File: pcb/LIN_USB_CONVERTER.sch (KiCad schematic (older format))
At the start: 33 parts, among them J1 Conn_01x03, J2 TerminalBlock, J3 GS2, J4 USB_A, J5 Conn_01x02, P2 CONN_01X05, U1 TJA1028TK/3V3/20/J, U2 MAX12931BASA+, U3 MCP1700T-3302E/TT, U4 STM32F042G4U6

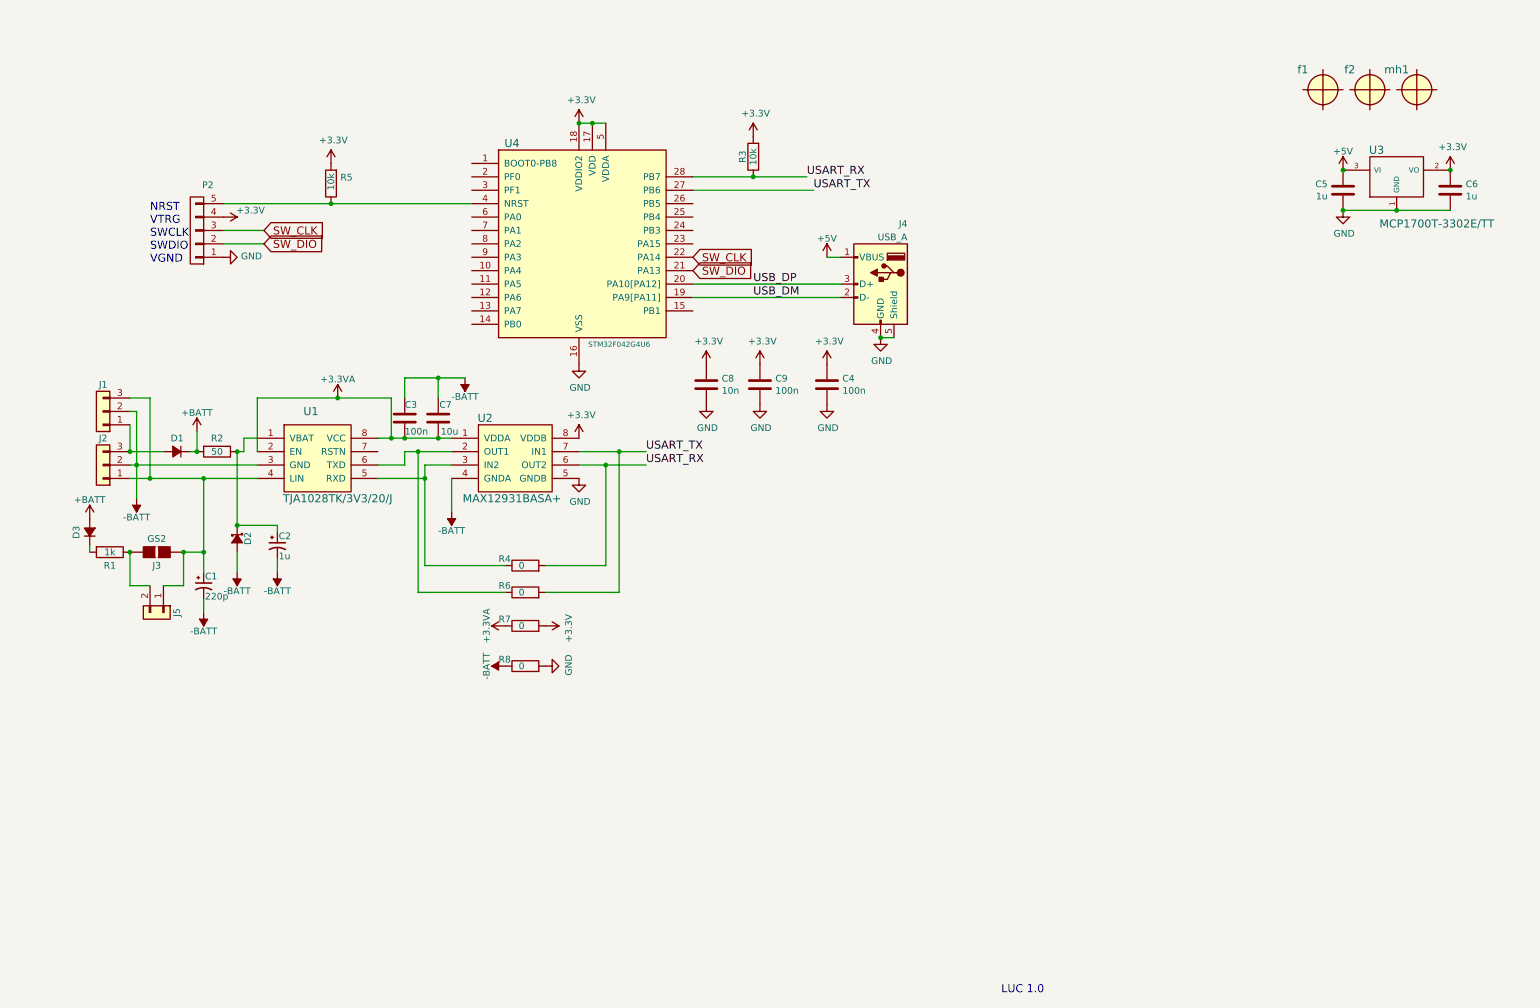
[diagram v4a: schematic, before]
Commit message: Remove of galvanic spearator
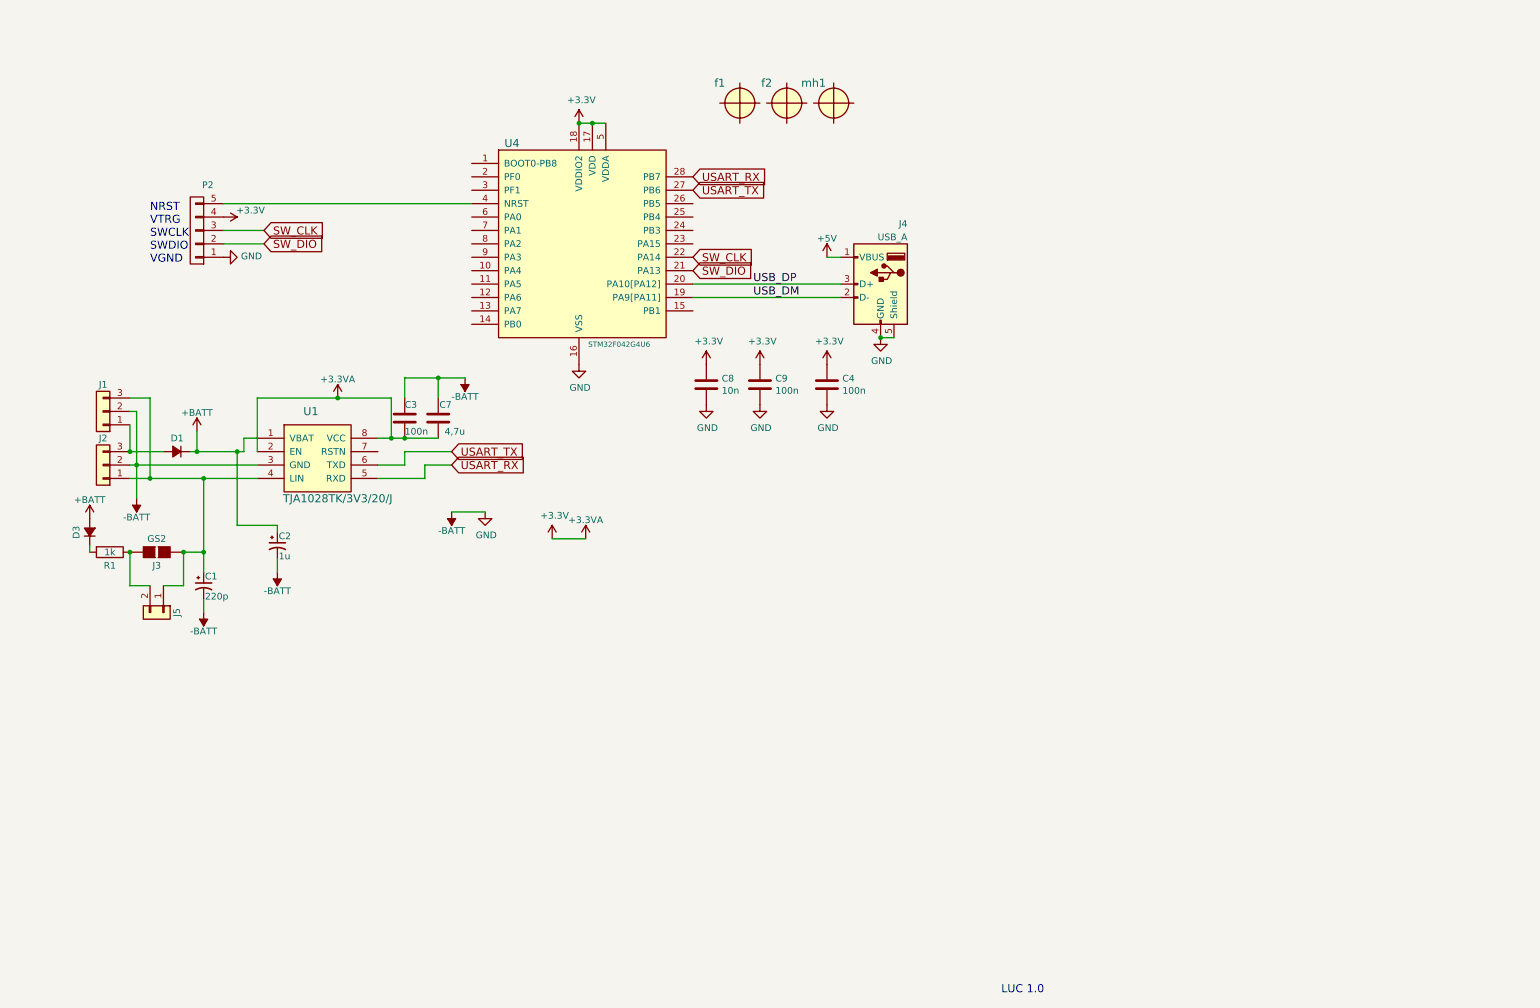
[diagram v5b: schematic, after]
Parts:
- removed C5, C6: 1u, Capacitors_SMD:C_0402, symbol LIN_USB_CONVERTER-rescue:C-RESCUE-LIN_USB_CONVERTER
- removed D2: 1N5819HW-7-F, Diodes_SMD:D_SOT-23_ANK, symbol LIN_USB_CONVERTER-rescue:D_Schottky_Small_ALT-RESCUE-LIN_USB_CONVERTER
- removed R2: 50, Resistors_SMD:R_0603, symbol LIN_USB_CONVERTER-rescue:R-RESCUE-LIN_USB_CONVERTER
- removed R3, R5: 10k, Resistors_SMD:R_0603, symbol LIN_USB_CONVERTER-rescue:R-RESCUE-LIN_USB_CONVERTER
- removed R4, R6, R7, R8: 0, Resistors_SMD:R_0603, symbol LIN_USB_CONVERTER-rescue:R-RESCUE-LIN_USB_CONVERTER
- removed U2: MAX12931BASA+, usb_ccb_custom:SOIC-8-N_MAXIM, symbol LIN_USB_CONVERTER-rescue:MAX12931-RESCUE-LIN_USB_CONVERTER
- removed U3: MCP1700T-3302E/TT, TO_SOT_Packages_SMD:SOT-23, symbol LIN_USB_CONVERTER-rescue:MCP1700T-3302E_TT-RESCUE-LIN_USB_CONVERTER
- C2: footprint Capacitors_SMD:C_0603 -> Capacitors_SMD:C_0805
- C7: value 10u -> 4,7u
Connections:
- net +3V3 is gone; now on net +3.3VA: C4.1, C8.1, C9.1, P2.4 (P4), U4.17 (VDD), U4.18 (VDDIO2), U4.5 (VDDA)
- net GND is gone; now on net -BATT: C4.2, C8.2, C9.2, J4.4 (GND), J4.5 (Shield), P2.1 (P1), U4.16 (VSS)
- net +BATT: now also C2.1, U1.1 (VBAT)
- net USART_RX: now also U1.5 (RXD)
- net USART_TX: now also U1.6 (TXD)
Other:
- moved on the sheet: f1, f2, mh1

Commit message: TJA package update
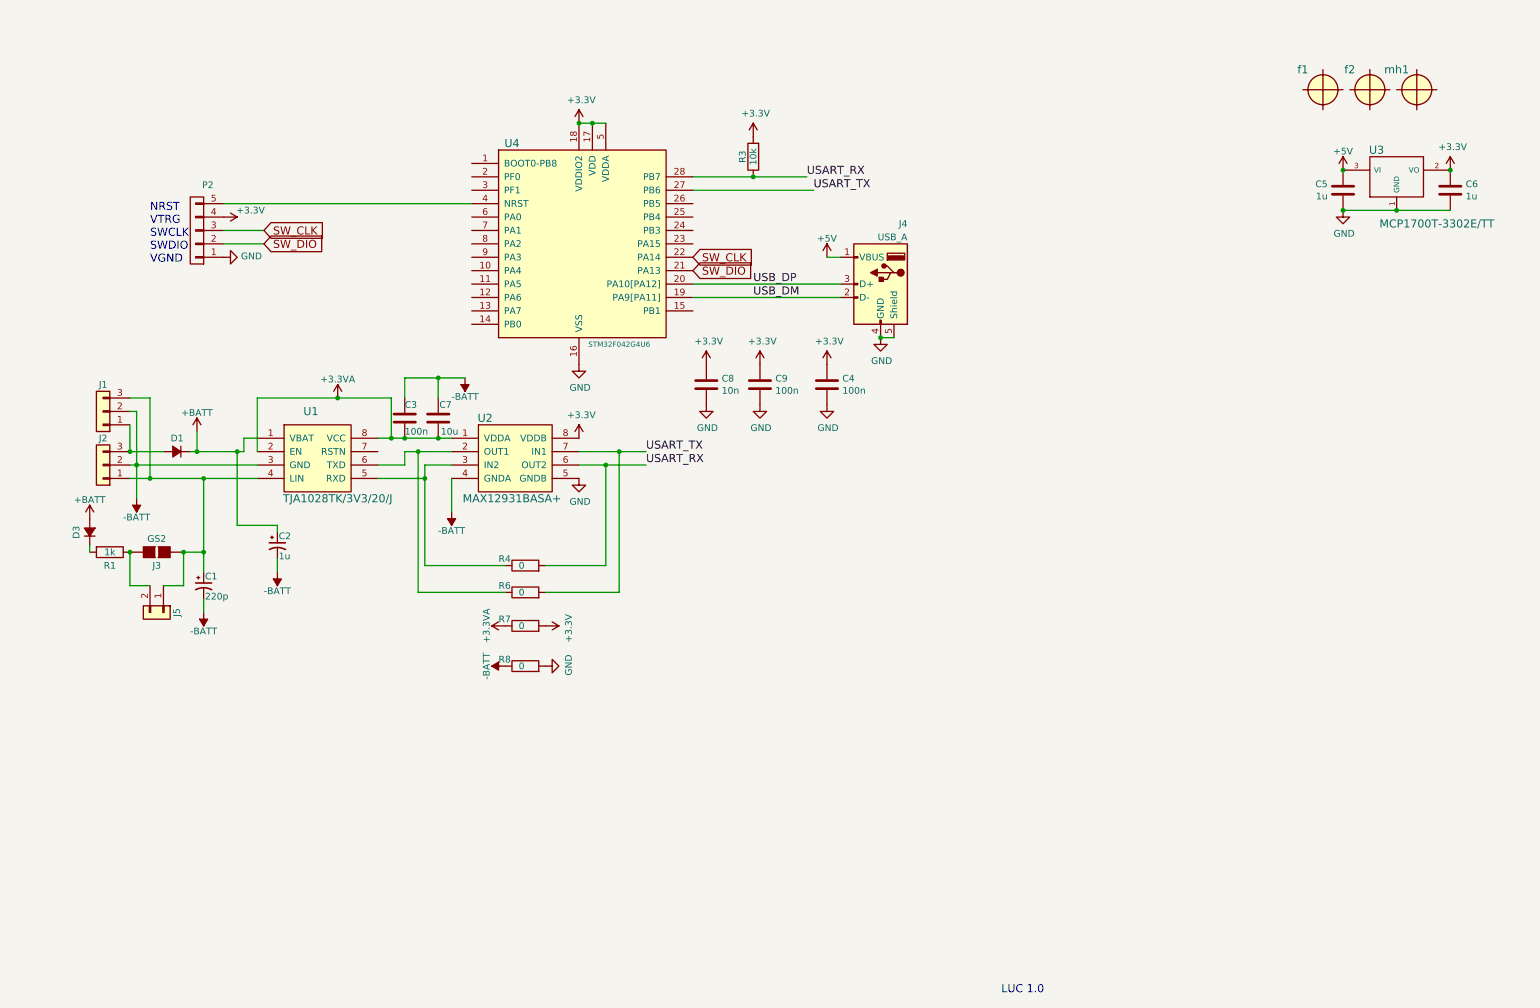
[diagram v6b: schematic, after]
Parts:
- added C5, C6: 1u, Capacitors_SMD:C_0603, symbol LIN_USB_CONVERTER-rescue:C-RESCUE-LIN_USB_CONVERTER
- added R3: 10k, Resistors_SMD:R_0603, symbol LIN_USB_CONVERTER-rescue:R-RESCUE-LIN_USB_CONVERTER
- added R4, R6, R7, R8: 0, Resistors_SMD:R_0603, symbol LIN_USB_CONVERTER-rescue:R-RESCUE-LIN_USB_CONVERTER
- added U2: MAX12931BASA+, usb_ccb_custom:SOIC-8-N_MAXIM, symbol LIN_USB_CONVERTER-rescue:MAX12931-RESCUE-LIN_USB_CONVERTER
- added U3: MCP1700T-3302E/TT, TO_SOT_Packages_SMD:SOT-23, symbol LIN_USB_CONVERTER-rescue:MCP1700T-3302E_TT-RESCUE-LIN_USB_CONVERTER
- C3, C4, C8, C9: footprint Capacitors_SMD:C_0402 -> Capacitors_SMD:C_0603
- C7: value 4,7u -> 10u; footprint Capacitors_SMD:C_0603 -> Capacitors_SMD:C_0805; 1st Disrtib Link https://www.tme.eu/pl/details/cl05a106mq5nunc/kondensatory-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 -> (none); Manufacturer SAMSUNG/CL05A106MQ5NUNC -> (none)
- U1: footprint usb_ccb_custom:HVSON8 -> Housings_SOIC:SOIC-8_3.9x4.9mm_Pitch1.27mm; 1st Disrtib Link https://octopart.com/tja1028tk%2F3v3%2F20%2Fj-nxp+semicondu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 -> (none)
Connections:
- net +3.3VA: now also R7.1, U2.1 (VDDA); no longer C4.1, C8.1, C9.1, P2.4 (P4), U4.17 (VDD), U4.18 (VDDIO2), U4.5 (VDDA)
- net +5V: now also C5.1, U3.3 (VI)
- net -BATT: now also R8.1, U2.4 (GNDA); no longer C4.2, C8.2, C9.2, J4.4 (GND), J4.5 (Shield), P2.1 (P1), U4.16 (VSS)
- net USART_RX: now also R3.1, R4.2, U2.6 (OUT2); no longer U1.5 (RXD)
- net USART_TX: now also R6.2, U2.7 (IN1); no longer U1.6 (TXD)
- new net: R4.1, U1.5 (RXD), U2.3 (IN2)
- new net: R6.1, U1.6 (TXD), U2.2 (OUT1)
- new net +3V3: C4.1, C6.1, C8.1, C9.1, P2.4 (P4), R3.2, R7.2, U2.8 (VDDB), U3.2 (VO), U4.17 (VDD), U4.18 (VDDIO2), U4.5 (VDDA)
- new net GND: C4.2, C5.2, C6.2, C8.2, C9.2, J4.4 (GND), J4.5 (Shield), P2.1 (P1), R8.2, U2.5 (GNDB), U3.1 (GND), U4.16 (VSS)
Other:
- moved on the sheet: f1, f2, mh1
